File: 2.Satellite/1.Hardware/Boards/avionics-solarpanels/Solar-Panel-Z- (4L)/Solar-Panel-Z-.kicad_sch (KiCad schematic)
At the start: 63 parts, among them J1 FTS-105-01-X-DV-A, J2 U.FL-R-SMT-1, Q5 IRLML2803, Q6 IRF7404, U1 BQ25570RGRR, U2 OPT3001, U3 MAX40200AUK

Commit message: update BOM
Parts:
- BA1: Manufacturer_Name (none) -> TDK Corporation; Manufacturer_Part_Number (none) -> ATB2012-50011-T000; Package/Footprint (none) -> 0805; Website (none) -> https://www.digikey.pt/pt/products/detail/tdk-corporation/A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
- C1: Manufacturer_Name (none) -> KYOCERA AVX; Manufacturer_Part_Number (none) -> 04025C104KAT2A; Package/Footprint (none) -> 0402; Website (none) -> https://www.digikey.pt/pt/products/detail/kyocera-avx/KGM05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
- C10, C11, C2, C9: Manufacturer_Name (none) -> KYOCERA AVX; Manufacturer_Part_Number (none) -> 06035C104K4T2A; Package/Footprint (none) -> 0603; Website (none) -> https://www.digikey.pt/pt/products/detail/kyocera-avx/KAM15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
- C3, C7: Manufacturer_Name (none) -> Murata Electronics; Manufacturer_Part_Number (none) -> GRT188R6YA475KE13D; Package/Footprint (none) -> 0603; Website (none) -> https://www.digikey.pt/pt/products/detail/murata-electronic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
- C4: Manufacturer_Name (none) -> KYOCERA AVX; Manufacturer_Part_Number (none) -> 06031C103K4T4A; Package/Footprint (none) -> 0603; Website (none) -> https://www.digikey.pt/pt/products/detail/kyocera-avx/KAM15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
- C5: Manufacturer_Name (none) -> Murata Electronics; Manufacturer_Part_Number (none) -> GRM21BR60J107ME15K; Package/Footprint (none) -> 0805; Website (none) -> https://www.digikey.pt/pt/products/detail/murata-electronic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
- C6: Manufacturer_Name (none) -> Murata Electronics; Manufacturer_Part_Number (none) -> GRT188R61H105KE13D; Package/Footprint (none) -> 0603; Website (none) -> https://www.digikey.pt/pt/products/detail/murata-electronic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
- C8: Manufacturer_Name (none) -> Murata Electronics; Manufacturer_Part_Number (none) -> GRT188R61A226ME13D; Package/Footprint (none) -> 0603; Website (none) -> https://www.digikey.pt/pt/products/detail/murata-electronic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
- D1: Manufacturer_Name (none) -> onsemi; Manufacturer_Part_Number (none) -> SZMM5Z5V1T1G; Package/Footprint (none) -> SOD-523; Website (none) -> https://www.digikey.pt/pt/products/detail/onsemi/SZMM5Z5V1T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
- D2, D3, D4: Manufacturer_Name (none) -> Diodes Incorporated; Manufacturer_Part_Number (none) -> DFLS130L-7; Package/Footprint (none) -> PowerDI-123; Website (none) -> https://www.digikey.pt/pt/products/detail/diodes-incorporat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
- J1: Manufacturer_Name (none) -> Samtec Inc.; Manufacturer_Part_Number (none) -> FTS-105-01-L-DV-A-P-TR; Website (none) -> https://www.digikey.pt/pt/products/detail/samtec-inc/FTS-10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
- J2: Manufacturer_Name Hirose -> Hirose Electric Co Ltd; Manufacturer_Part_Number U.FL-R-SMT-1 -> U.FL-R-SMT-1(10); Website (none) -> https://www.digikey.pt/pt/products/detail/hirose-electric-c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
- L1: Manufacturer_Name (none) -> Coilcraft; Manufacturer_Part_Number (none) -> LPS4018-223MRC; Package/Footprint (none) -> 1515; Website (none) -> https://www.digikey.pt/pt/products/detail/coilcraft/LPS4018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
- L2: Manufacturer_Name (none) -> Coilcraft; Manufacturer_Part_Number (none) -> LPS4018-103MRC; Package/Footprint (none) -> 1515; Website (none) -> https://www.digikey.pt/pt/products/detail/coilcraft/LPS4018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
- Q5: Flight IRLML2803 -> (none); Manufacturer_Name (none) -> Infineon Technologies; Manufacturer_Part_Number (none) -> IRLML2803TRPBF; Package/Footprint (none) -> SOT-23-3; Proto 2302 -> (none); Website (none) -> https://www.digikey.pt/pt/products/detail/infineon-technolo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
- Q6: Manufacturer_Name (none) -> Infineon Technologies; Manufacturer_Part_Number (none) -> IRF7404TRPBF; Package/Footprint (none) -> 8-SOIC; Website (none) -> https://www.digikey.pt/pt/products/detail/infineon-technolo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
- R1, R2: Manufacturer_Name (none) -> Stackpole Electronics Inc; Manufacturer_Part_Number (none) -> RMCF0402ZT0R00; Package/Footprint (none) -> 0402; Website (none) -> https://www.digikey.pt/pt/products/detail/stackpole-electro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
- R10, R8: Manufacturer_Name (none) -> Vishay Dale; Manufacturer_Part_Number (none) -> CRCW06038M25FKEA; Package/Footprint (none) -> 0603; Website (none) -> https://www.digikey.pt/pt/products/detail/vishay-dale/CRCW0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
- R11: Manufacturer_Name (none) -> Stackpole Electronics Inc; Manufacturer_Part_Number (none) -> RMCF0603FT4M75; Package/Footprint (none) -> 0603; Website (none) -> https://www.digikey.pt/pt/products/detail/stackpole-electro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
- R12, R13, R16, R17, R18, R3, R4: Manufacturer_Name (none) -> Stackpole Electronics Inc; Manufacturer_Part_Number (none) -> RMCF0603ZT0R00; Package/Footprint (none) -> 0603; Website (none) -> https://www.digikey.pt/pt/products/detail/stackpole-electro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
- R31: Manufacturer_Name (none) -> Stackpole Electronics Inc; Manufacturer_Part_Number (none) -> RNCF0603BTE10K0; Package/Footprint (none) -> 0603; Website (none) -> https://www.digikey.pt/pt/products/detail/stackpole-electro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
- R32: Manufacturer_Name (none) -> Stackpole Electronics Inc; Manufacturer_Part_Number (none) -> RNCF0603DTE4K70; Package/Footprint (none) -> 0603; Website (none) -> https://www.digikey.pt/pt/products/detail/stackpole-electro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
- R33: Manufacturer_Name (none) -> Stackpole Electronics Inc; Manufacturer_Part_Number (none) -> RNCF0603DTE100K; Package/Footprint (none) -> 0603; Website (none) -> https://www.digikey.pt/pt/products/detail/stackpole-electro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
- R34: Manufacturer_Name (none) -> Stackpole Electronics Inc; Manufacturer_Part_Number (none) -> RNCF1206DTE1R00; Package/Footprint (none) -> 1206; Website (none) -> https://www.digikey.pt/pt/products/detail/stackpole-electro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
- R5: Manufacturer_Name (none) -> Stackpole Electronics Inc; Manufacturer_Part_Number (none) -> RMCF0603FT7M32; Package/Footprint (none) -> 0603; Website (none) -> https://www.digikey.pt/pt/products/detail/stackpole-electro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
- R6: Manufacturer_Name (none) -> Stackpole Electronics Inc; Manufacturer_Part_Number (none) -> RMCF0603FT5M62; Package/Footprint (none) -> 0603; Website (none) -> https://www.digikey.pt/pt/products/detail/stackpole-electro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
- R7: Manufacturer_Name (none) -> Stackpole Electronics Inc; Manufacturer_Part_Number (none) -> RMCF0603FT374K; Package/Footprint (none) -> 0603; Website (none) -> https://www.digikey.pt/pt/products/detail/stackpole-electro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
- R9: Manufacturer_Name (none) -> Stackpole Electronics Inc; Manufacturer_Part_Number (none) -> RMCF0603FT4M53; Package/Footprint (none) -> 0603; Website (none) -> https://www.digikey.pt/pt/products/detail/stackpole-electro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
- SC1, SC2, SC3, SC4: Manufacturer_Name (none) -> ANYSOLAR Ltd; Manufacturer_Part_Number (none) -> KXOB25-05X3F-TR; Website (none) -> https://www.digikey.pt/pt/products/detail/anysolar-ltd/KXOB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
- U1: Manufacturer_Name (none) -> Texas Instruments; Manufacturer_Part_Number (none) -> BQ25570RGRR; Package/Footprint (none) -> 20-VQFN; Website (none) -> https://www.digikey.pt/pt/products/detail/texas-instruments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
- U2: Manufacturer_Name (none) -> Texas Instruments; Manufacturer_Part_Number (none) -> OPT3001IDNPRQ1; Package/Footprint (none) -> 6-USON; Website (none) -> https://www.digikey.pt/pt/products/detail/texas-instruments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
- U3: Manufacturer_Name (none) -> Analog Devices Inc./Maxim Integrated; Manufacturer_Part_Number (none) -> MAX40200AUK+T; Package/Footprint (none) -> SOT-23-5; Website (none) -> https://www.digikey.pt/pt/products/detail/analog-devices-in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

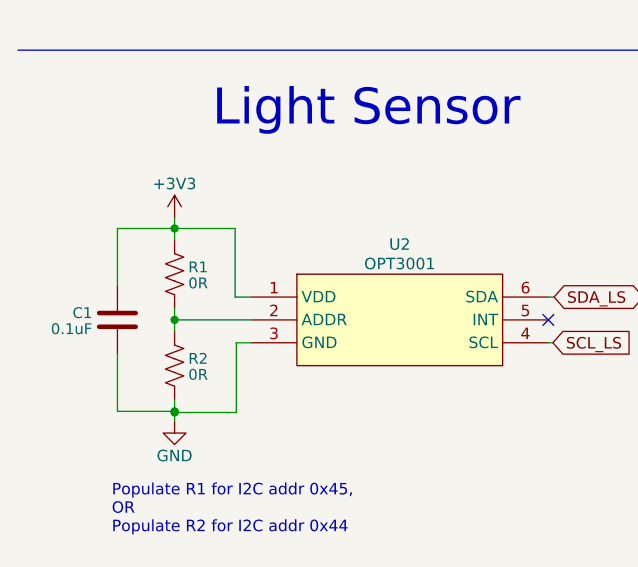
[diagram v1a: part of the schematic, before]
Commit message: Updated I2C address resistors; Added reference to KiCad docs
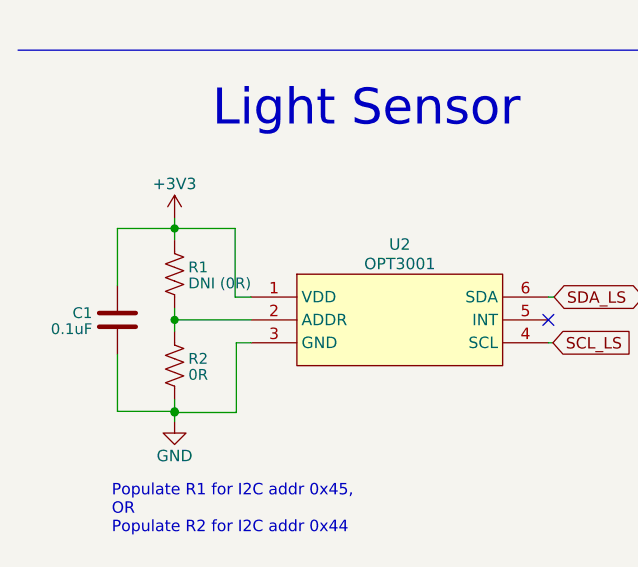
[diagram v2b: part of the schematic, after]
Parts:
- R1: value 0R -> DNI (0R); DNI (none) -> DNI
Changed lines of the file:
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@@
       (effects (font (size 1.2 1.2)) (justify right))
     )
-    (property "Value" "0R" (at 30.353 171.958 0)
+    (property "Value" "DNI (0R)" (at 30.353 171.958 0)
       (effects (font (size 1.2 1.2)) (justify right))
     )
@@
       (effects (font (size 1.27 1.27)) hide)
     )
+    (property "DNI" "DNI" (at 28.829 170.942 0)
+      (effects (font (size 1.27 1.27)) hide)
+    )
